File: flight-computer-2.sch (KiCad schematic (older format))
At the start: 80 parts

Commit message: Connecting interrupt pins
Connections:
- wire segments 211 -> 214
- no-connect marks 32 -> 29
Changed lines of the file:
@@
 Sheet 1 1
 Title "VTOL EDF Flight Computer"
-Date "2020-07-23"
+Date "2020-07-24"
 Rev "v2"
 Comp ""
@@
 NoConn ~ 9400 1750
 NoConn ~ 9400 1850
-NoConn ~ 7800 2650
-NoConn ~ 7800 2550
 NoConn ~ 9400 2250
 NoConn ~ 9400 2150
@@
 Wire Wire Line
 	4050 1900 4200 1900
-NoConn ~ 7800 2950
 Text Label 9550 2350 2    50   ~ 0
 IO10
@@
 Connection ~ 2600 5550
 Connection ~ 2600 5850
+Text Label 7500 2950 0    50   ~ 0
+IMU_INT
+Wire Wire Line
+	7500 2950 7800 2950
+Text Label 7450 2650 0    50   ~ 0
+ALT_INT_1
+Text Label 7450 2550 0    50   ~ 0
+ALT_INT_2
+Wire Wire Line
+	7450 2550 7800 2550
+Wire Wire Line
+	7450 2650 7800 2650
 $EndSCHEMATC

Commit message: Assigning footprints
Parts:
- D1, D3: renamed from D?; footprint (none) -> flight-computer-2:D_PowerDI-5
- D4, D5, D6: renamed from D?; footprint (none) -> flight-computer-2:D_SOD-523
- D9: renamed from D?; footprint (none) -> flight-computer-2:LED_Cree-PLCC4_2x2mm_CW
- E1: renamed from E?; footprint (none) -> flight-computer-2:ANT_PRO-OB-440
- J1: renamed from J?; footprint (none) -> flight-computer-2:GCT_USB4105-GF-A
- J2, J3, J4, J5, J6: renamed from J?; footprint (none) -> flight-computer-2:PinHeader_1x03_P2.54mm_Vertical
- J7, J8: renamed from J?; footprint (none) -> flight-computer-2:PinHeader_1x07_P2.54mm_Vertical
- SW1, SW2: renamed from SW?; footprint (none) -> flight-computer-2:SW_PTS810_SJM_250_SMTR_LFS
- U1: renamed from U?; footprint (none) -> flight-computer-2:SOT-223
- U2: renamed from U?; footprint (none) -> flight-computer-2:SOT-363_SC-70-6
- U3: renamed from U?; footprint (none) -> flight-computer-2:LGA-28_5.2x3.8mm_P0.5mm
- U4: renamed from U?; footprint (none) -> flight-computer-2:QFN-28-1EP_5x5mm_P0.5mm_EP3.35x3.35mm
- U5: renamed from U?; footprint (none) -> flight-computer-2:LGA-8_3x5mm_P1.25mm
- U6: renamed from U?; footprint (none) -> flight-computer-2:PQFN50P700X700X104-49N
- Y1: renamed from Y?; footprint (none) -> flight-computer-2:ABS07
- gave numbers to parts that had none: 56

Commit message: New USB ESD protection IC
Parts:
- removed D4, D5, D6: ESD5Z5.0T1G, flight-computer-2:D_SOD-523, symbol Device:D_TVS_ALT
- added D?: USBLC6-2SC6, Package_TO_SOT_SMD:SOT-23-6, symbol flight-computer-2:USBLC6-2SC6
- added R?: 1M, symbol Device:R_Small
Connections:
- wire segments 214 -> 219
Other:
- moved on the sheet: D3
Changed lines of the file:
@@
 $EndComp
 Wire Wire Line
-	1600 5750 1500 5750
-Wire Wire Line
-	1600 5950 1500 5950
-Connection ~ 1500 5950
+	1400 5950 1300 5950
+Connection ~ 1300 5950
 NoConn ~ 1600 5150
 NoConn ~ 1600 5250
@@
 	0    -1   -1   0
 $EndComp
-Wire Wire Line
-	2500 5450 2600 5450
-Wire Wire Line
-	2600 5450 2600 5550
-Wire Wire Line
-	2600 5550 2500 5550
-Wire Wire Line
-	2500 5750 2600 5750
-Wire Wire Line
-	2600 5750 2600 5850
-Wire Wire Line
-	2600 5850 2500 5850
-Text Label 3300 5150 2    50   ~ 0
+Text Label 3300 5050 2    50   ~ 0
 VIN
 Wire Wire Line
-	3300 5150 3150 5150
-$Comp
-L Device:D_TVS_ALT D6
-U 1 1 5F108BF7
-P 3000 5850
-F 0 "D6" H 3000 6000 50  0000 C CNN
-F 1 "ESD5Z5.0T1G" H 3000 6100 50  0000 C CNN
-F 2 "flight-computer-2:D_SOD-523" H 3000 5850 50  0001 C CNN
-F 3 "~" H 3000 5850 50  0001 C CNN
-F 4 "ESD5Z5.0T1G" H 3000 5850 50  0001 C CNN "MPN"
-	1    3000 5850
-	-1   0    0    1
-$EndComp
+	3300 5050 3150 5050
 $Comp
 L Device:D_Schottky_ALT D3
 U 1 1 5F10A2FB
-P 3000 5150
-F 0 "D3" H 3000 4934 50  0000 C CNN
-F 1 "PDS4150-13" H 3000 5025 50  0000 C CNN
-F 2 "flight-computer-2:D_PowerDI-5" H 3000 5150 50  0001 C CNN
-F 3 "~" H 3000 5150 50  0001 C CNN
-F 4 "PDS4150-13" H 3000 5150 50  0001 C CNN "MPN"
-	1    3000 5150
+P 3000 5050
+F 0 "D3" H 3000 4834 50  0000 C CNN
+F 1 "PDS4150-13" H 3000 4925 50  0000 C CNN
+F 2 "flight-computer-2:D_PowerDI-5" H 3000 5050 50  0001 C CNN
+F 3 "~" H 3000 5050 50  0001 C CNN
+F 4 "PDS4150-13" H 3000 5050 50  0001 C CNN "MPN"
+	1    3000 5050
 	-1   0    0    1
 $EndComp
-Wire Wire Line
-	2600 5550 2850 5550
-Wire Wire Line
-	2600 5850 2850 5850
-$Comp
-L Device:D_TVS_ALT D5
-U 1 1 5F11064B
-P 3000 5550
-F 0 "D5" H 3000 5650 50  0000 C CNN
-F 1 "ESD5Z5.0T1G" H 3000 5750 50  0000 C CNN
-F 2 "flight-computer-2:D_SOD-523" H 3000 5550 50  0001 C CNN
-F 3 "~" H 3000 5550 50  0001 C CNN
-F 4 "ESD5Z5.0T1G" H 3000 5550 50  0001 C CNN "MPN"
-	1    3000 5550
-	-1   0    0    1
-$EndComp
-Text Label 2700 5850 0    50   ~ 0
+Text Label 3400 5750 2    50   ~ 0
 D-
-Text Label 2700 5550 0    50   ~ 0
+Text Label 3400 5550 2    50   ~ 0
 D+
 $Comp
@@
 $EndComp
 Wire Wire Line
-	1500 5750 1500 5850
-Wire Wire Line
-	1600 5850 1500 5850
-Connection ~ 1500 5850
-Wire Wire Line
-	1500 5850 1500 5950
+	1300 5750 1300 5850
+Connection ~ 1300 5850
+Wire Wire Line
+	1300 5850 1300 5950
 $Comp
 L power:GND #PWR0118
 U 1 1 5F2FC5FB
-P 1500 6050
-F 0 "#PWR0118" H 1500 5800 50  0001 C CNN
-F 1 "GND" H 1505 5877 50  0000 C CNN
-F 2 "" H 1500 6050 50  0001 C CNN
-F 3 "" H 1500 6050 50  0001 C CNN
-	1    1500 6050
+P 1300 6050
+F 0 "#PWR0118" H 1300 5800 50  0001 C CNN
+F 1 "GND" H 1305 5877 50  0000 C CNN
+F 2 "" H 1300 6050 50  0001 C CNN
+F 3 "" H 1300 6050 50  0001 C CNN
+	1    1300 6050
 	1    0    0    -1
 $EndComp
@@
 $EndComp
 $Comp
-L Device:D_TVS_ALT D4
-U 1 1 5F10B283
-P 3000 5250
-F 0 "D4" H 2950 5350 50  0000 L CNN
-F 1 "ESD5Z5.0T1G" H 2750 5450 50  0000 L CNN
-F 2 "flight-computer-2:D_SOD-523" H 3000 5250 50  0001 C CNN
-F 3 "~" H 3000 5250 50  0001 C CNN
-F 4 "ESD5Z5.0T1G" H 3000 5250 50  0001 C CNN "MPN"
-	1    3000 5250
-	-1   0    0    1
-$EndComp
-$Comp
 L power:GND #PWR0119
 U 1 1 5F384159
@@
 $EndComp
 Connection ~ 8050 6050
-$Comp
-L power:GND #PWR0120
-U 1 1 5F3CFF34
-P 3150 5250
-F 0 "#PWR0120" H 3150 5000 50  0001 C CNN
-F 1 "GND" V 3155 5122 50  0000 R CNN
-F 2 "" H 3150 5250 50  0001 C CNN
-F 3 "" H 3150 5250 50  0001 C CNN
-	1    3150 5250
-	0    -1   -1   0
-$EndComp
-$Comp
-L power:GND #PWR0121
-U 1 1 5F3D04B5
-P 3150 5550
-F 0 "#PWR0121" H 3150 5300 50  0001 C CNN
-F 1 "GND" V 3155 5422 50  0000 R CNN
-F 2 "" H 3150 5550 50  0001 C CNN
-F 3 "" H 3150 5550 50  0001 C CNN
-	1    3150 5550
-	0    -1   -1   0
-$EndComp
-$Comp
-L power:GND #PWR0122
-U 1 1 5F3D0830
-P 3150 5850
-F 0 "#PWR0122" H 3150 5600 50  0001 C CNN
-F 1 "GND" V 3155 5722 50  0000 R CNN
-F 2 "" H 3150 5850 50  0001 C CNN
-F 3 "" H 3150 5850 50  0001 C CNN
-	1    3150 5850
-	0    -1   -1   0
-$EndComp
 $Comp
 L flight-computer-2:ESP32-PICO-D4 U6
@@
 Connection ~ 2700 1400
 Wire Wire Line
-	1500 5950 1500 6050
-Wire Wire Line
-	2850 5150 2850 5250
+	1300 5950 1300 6050
+Wire Wire Line
+	2850 5050 2850 5150
 Wire Wire Line
 	2500 5150 2600 5150
@@
 	2600 5250 2500 5250
 Wire Wire Line
-	2600 5250 2850 5250
-Connection ~ 2850 5250
+	2600 5150 2850 5150
 $Comp
 L power:PWR_FLAG #FLG0101
@@
 Wire Wire Line
 	9900 1450 10250 1450
-Connection ~ 2600 5250
-Connection ~ 2600 5550
-Connection ~ 2600 5850
 Text Label 7500 2950 0    50   ~ 0
 IMU_INT
@@
 Wire Wire Line
 	7450 2650 7800 2650
+$Comp
+L Device:R_Small R?
+U 1 1 5F20CB9C
+P 1500 5950
+F 0 "R?" V 1400 5950 50  0000 C CNN
+F 1 "1M" V 1300 5950 50  0000 C CNN
+F 2 "" H 1500 5950 50  0001 C CNN
+F 3 "~" H 1500 5950 50  0001 C CNN
+	1    1500 5950
+	0    -1   -1   0
+$EndComp
+Wire Wire Line
+	1300 5750 1600 5750
+Wire Wire Line
+	1300 5850 1600 5850
+Wire Wire Line
+	2500 5450 2600 5450
+Wire Wire Line
+	2600 5450 2600 5550
+Wire Wire Line
+	2600 5550 2500 5550
+Wire Wire Line
+	2500 5750 2600 5750
+Wire Wire Line
+	2600 5750 2600 5850
+Wire Wire Line
+	2600 5850 2500 5850
+Connection ~ 2600 5550
+$Comp
+L flight-computer-2:USBLC6-2SC6 D?
+U 1 1 5F45F25E
+P 3000 5850
+F 0 "D?" H 3000 5750 50  0000 C CNN
+F 1 "USBLC6-2SC6" H 3000 5650 50  0000 C CNN
+F 2 "Package_TO_SOT_SMD:SOT-23-6" H 3200 5850 50  0001 L BNN
+F 3 "~" H 3200 5850 50  0001 L BNN
+	1    3000 5850
+	1    0    0    -1
+$EndComp
+Wire Wire Line
+	2600 5550 2700 5550
+Connection ~ 2600 5150
+$Comp
+L power:GND #PWR?
+U 1 1 5F510CC3
+P 2700 5350
+F 0 "#PWR?" H 2700 5100 50  0001 C CNN
+F 1 "GND" V 2705 5222 50  0000 R CNN
+F 2 "" H 2700 5350 50  0001 C CNN
+F 3 "" H 2700 5350 50  0001 C CNN
+	1    2700 5350
+	0    1    1    0
+$EndComp
+Wire Wire Line
+	2600 5750 2700 5750
+Connection ~ 2600 5750
+Wire Wire Line
+	2850 5150 3400 5150
+Connection ~ 2850 5150
+Wire Wire Line
+	3300 5350 3400 5350
+Wire Wire Line
+	3400 5350 3400 5150
+Wire Wire Line
+	3300 5550 3400 5550
+Wire Wire Line
+	3300 5750 3400 5750
 $EndSCHEMATC

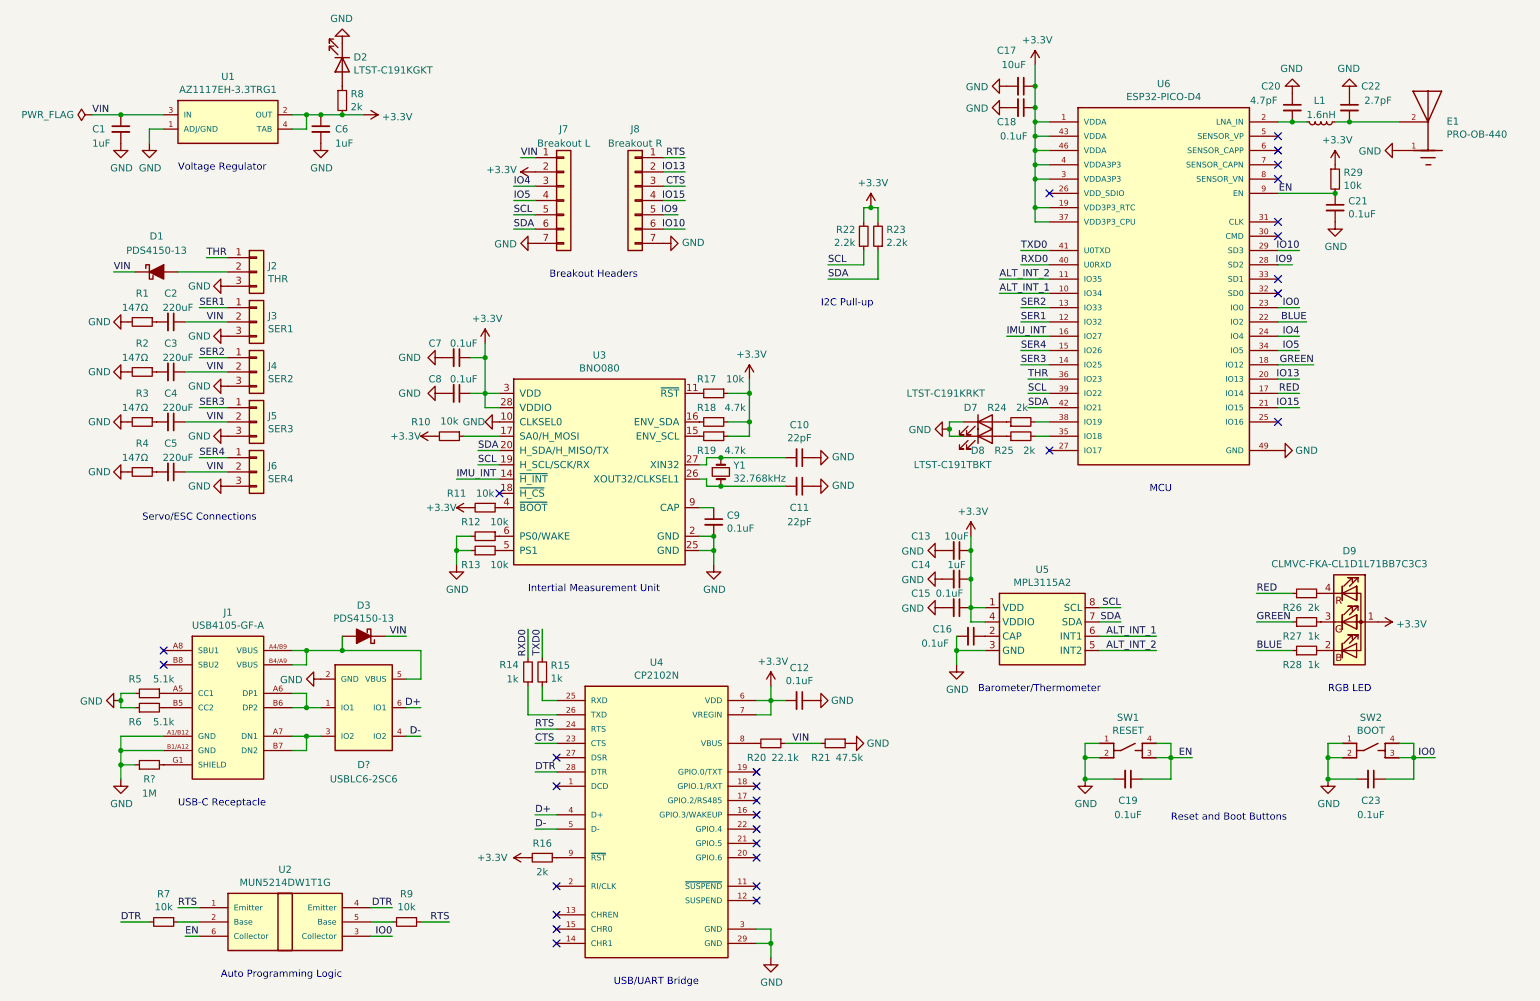
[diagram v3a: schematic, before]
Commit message: New antenna
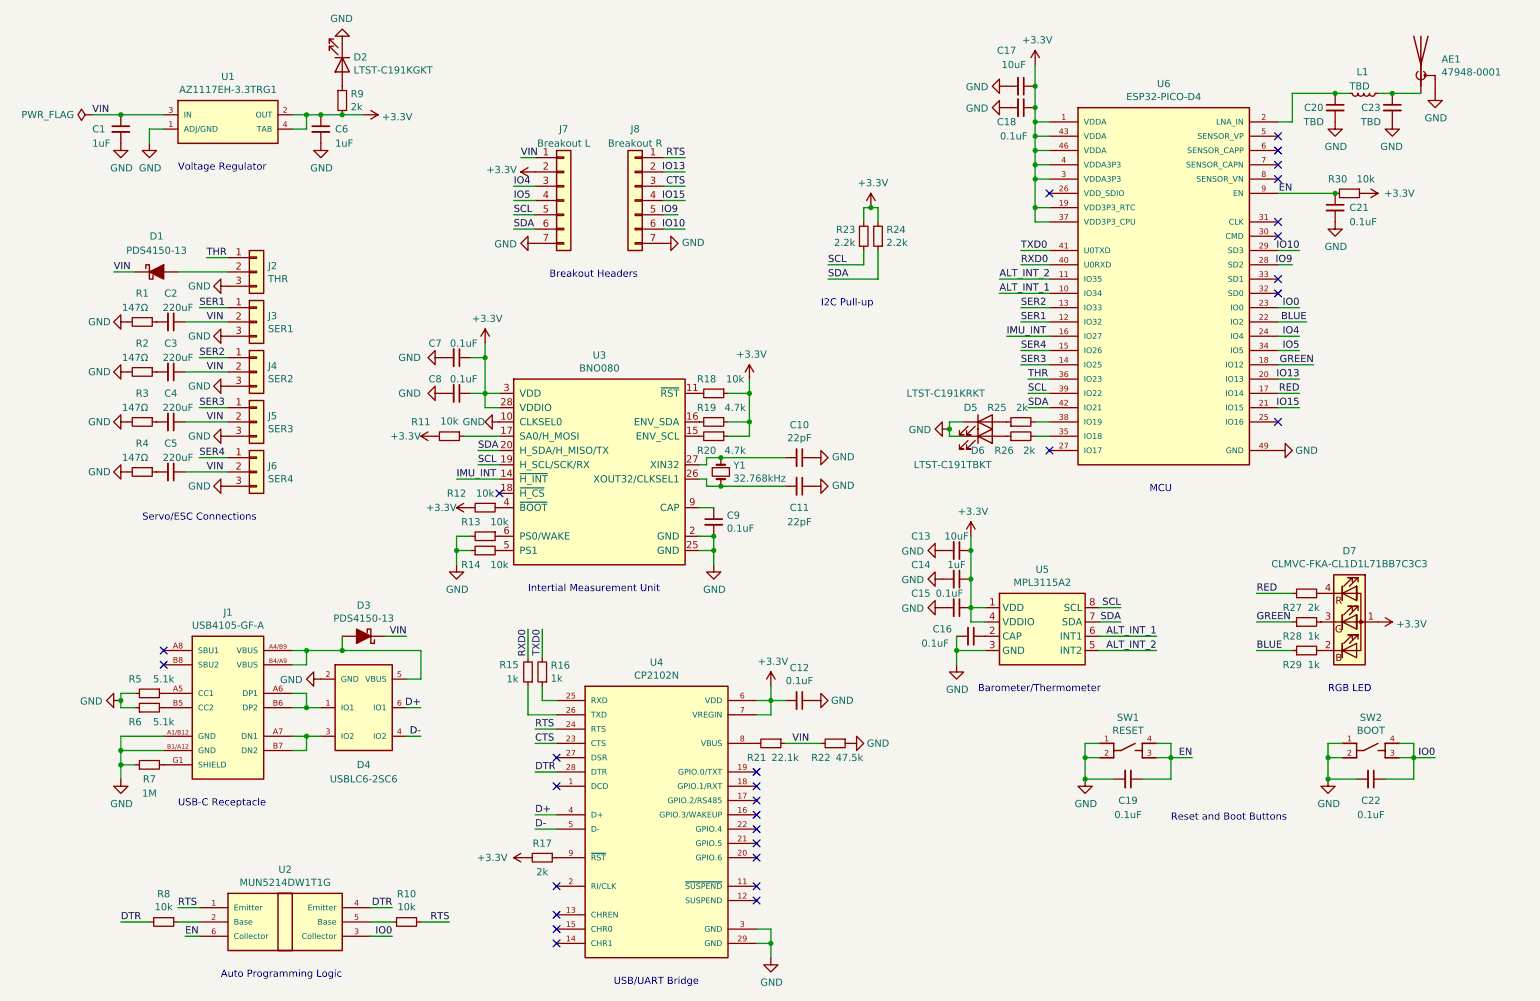
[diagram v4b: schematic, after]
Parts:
- removed E1: PRO-OB-440, flight-computer-2:ANT_PRO-OB-440, symbol flight-computer-2:PRO-OB-440
- added AE1: 47948-0001, symbol flight-computer-2:47948-0001
- C20: value 4.7pF -> TBD
- C23: renamed from C22; value 2.7pF -> TBD
- D4: renamed from D?; MPN (none) -> USBLC6-2SC6
- L1: value 1.6nH -> TBD
- gave numbers to parts that had none: 1
- renumbered C23 to C22, D7 to D5, D8 to D6, D9 to D7, R9 to R10, R10 to R11, R11 to R12, R12 to R13, R13 to R14, R14 to R15, R15 to R16, R16 to R17, R17 to R18, R18 to R19, R19 to R20, R20 to R21, R21 to R22, R22 to R23, R23 to R24, R24 to R25, R25 to R26, R26 to R27, R27 to R28, R28 to R29, R29 to R30, R7 to R8, R8 to R9
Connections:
- net GND: now also C20.2, C23.2, AE1.2 (PAD1), AE1.3 (PAD2), AE1.4 (PAD3); no longer C20.1, C23.1
- net at L1.2, U6.2 (LNA_IN): now also C20.1; no longer C20.2
- net at L1.1: now also C23.1, AE1.1 (FEED); no longer C23.2
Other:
- moved on the sheet: C20, C23, L1, R30

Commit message: Assigning footprints
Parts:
- AE1: footprint (none) -> flight-computer-2:47948-0001
- C1, C10, C11, C12, C13, C14, C15, C16, C17, C18, C19, C2, C21, C22, C3, C4, C5, C6, C7, C8, C9: footprint (none) -> flight-computer-2:C_0603_1608Metric
- C20, C23: value TBD -> DNP; footprint (none) -> flight-computer-2:C_0402_1005Metric
- D2, D5, D6: footprint (none) -> flight-computer-2:LED_0603_1608Metric
- L1: value TBD -> 0K; footprint (none) -> flight-computer-2:L_0402_1005Metric
- R1, R10, R11, R12, R13, R14, R15, R16, R17, R18, R19, R2, R20, R21, R22, R23, R24, R25, R26, R27, R28, R29, R3, R30, R4, R5, R6, R7, R8, R9: footprint (none) -> flight-computer-2:R_0603_1608Metric

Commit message: New voltage regulator and diode
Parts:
- C1, C6: value 1uF -> 4.7uF
- D1, D3: value PDS4150-13 -> SM5817PL-TP
- U1: value AZ1117EH-3.3TRG1 -> AP2114H-3.3TRG1; symbol flight-computer-2:AZ1117EH-3.3TRG1 -> flight-computer-2:AP2114H-3.3TRG1; MPN AZ1117EH-3.3TRG1 -> AP2114H-3.3TRG1
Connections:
- net IO5: no longer J7.4 (Pin_4), U6.34 (IO5)
- net VIN: no longer C2.1, C3.1, C4.1, C5.1, J3.2 (Pin_2), J4.2 (Pin_2), J5.2 (Pin_2), J6.2 (Pin_2)
- net VBEC: now reaches D1.2 (A), J2.2 (Pin_2)
- net VBEC: now also C2.1, C3.1, C4.1, C5.1, J3.2 (Pin_2), J4.2 (Pin_2), J5.2 (Pin_2), J6.2 (Pin_2)
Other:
- moved on the sheet: D1
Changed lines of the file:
@@
 P 3000 5050
 F 0 "D3" H 3000 4834 50  0000 C CNN
-F 1 "PDS4150-13" H 3000 4925 50  0000 C CNN
+F 1 "SM5817PL-TP" H 3000 4925 50  0000 C CNN
 F 2 "flight-computer-2:D_PowerDI-5" H 3000 5050 50  0001 C CNN
 F 3 "~" H 3000 5050 50  0001 C CNN
@@
 P 2700 1500
 F 0 "C6" H 2800 1500 50  0000 L CNN
-F 1 "1uF" H 2800 1400 50  0000 L CNN
+F 1 "4.7uF" H 2800 1400 50  0000 L CNN
 F 2 "flight-computer-2:C_0603_1608Metric" H 2700 1500 50  0001 C CNN
 F 3 "~" H 2700 1500 50  0001 C CNN
@@
 P 1300 1500
 F 0 "C1" H 1100 1500 50  0000 L CNN
-F 1 "1uF" H 1100 1400 50  0000 L CNN
+F 1 "4.7uF" H 1050 1400 50  0000 L CNN
 F 2 "flight-computer-2:C_0603_1608Metric" H 1300 1500 50  0001 C CNN
 F 3 "~" H 1300 1500 50  0001 C CNN
@@
 $EndComp
 $Comp
-L flight-computer-2:AZ1117EH-3.3TRG1 U1
+L flight-computer-2:AP2114H-3.3TRG1 U1
 U 1 1 5F13844B
 P 2050 1500
 F 0 "U1" H 2050 1867 50  0000 C CNN
-F 1 "AZ1117EH-3.3TRG1" H 2050 1776 50  0000 C CNN
+F 1 "AP2114H-3.3TRG1" H 2050 1776 50  0000 C CNN
 F 2 "flight-computer-2:SOT-223" H 1650 1300 50  0001 L BNN
 F 3 "~" H 2000 1200 50  0001 L BNN
-F 4 "AZ1117EH-3.3TRG1" H 2050 1500 50  0001 C CNN "MPN"
+F 4 "AP2114H-3.3TRG1" H 2050 1500 50  0001 C CNN "MPN"
 	1    2050 1500
 	1    0    0    -1
@@
 L Device:D_Schottky_ALT D1
 U 1 1 5F77575B
-P 1550 2500
-F 0 "D1" H 1550 2750 50  0000 C CNN
-F 1 "PDS4150-13" H 1550 2650 50  0000 C CNN
-F 2 "flight-computer-2:D_PowerDI-5" H 1550 2500 50  0001 C CNN
-F 3 "~" H 1550 2500 50  0001 C CNN
-F 4 "PDS4150-13" H 1550 2500 50  0001 C CNN "MPN"
-	1    1550 2500
-	1    0    0    -1
-$EndComp
-Text Label 1250 2500 0    50   ~ 0
-VIN
-Wire Wire Line
-	1250 2500 1400 2500
-Wire Wire Line
-	1700 2500 2050 2500
+P 1600 2500
+F 0 "D1" H 1600 2750 50  0000 C CNN
+F 1 "SM5817PL-TP" H 1600 2650 50  0000 C CNN
+F 2 "flight-computer-2:D_PowerDI-5" H 1600 2500 50  0001 C CNN
+F 3 "~" H 1600 2500 50  0001 C CNN
+F 4 "PDS4150-13" H 1600 2500 50  0001 C CNN "MPN"
+	1    1600 2500
+	1    0    0    -1
+$EndComp
+Wire Wire Line
+	1750 2500 2050 2500
 $Comp
 L power:GND #PWR09
@@
 $EndComp
 Text Label 1900 2850 0    50   ~ 0
-VIN
+VBEC
 Text Label 1900 3200 0    50   ~ 0
-VIN
+VBEC
 Text Label 1900 3550 0    50   ~ 0
-VIN
+VBEC
 Text Label 1900 3900 0    50   ~ 0
-VIN
+VBEC
 Wire Wire Line
 	1750 2850 2050 2850
@@
 Text Label 9550 2950 2    50   ~ 0
 IO4
-Text Label 9550 3050 2    50   ~ 0
+Text Label 9950 3050 2    50   ~ 0
 IO5
 Wire Wire Line
 	9400 2950 9550 2950
 Wire Wire Line
-	9400 3050 9550 3050
+	9800 3050 9950 3050
 Text Label 4050 1900 0    50   ~ 0
 IO4
-Text Label 4050 2000 0    50   ~ 0
+Text Label 3650 2000 0    50   ~ 0
 IO5
 Wire Wire Line
-	4050 2000 4200 2000
+	3650 2000 3800 2000
 Wire Wire Line
 	4050 1900 4200 1900
@@
 $EndComp
 Connection ~ 9800 1950
+Text Label 1900 2500 0    50   ~ 0
+VBEC
+Wire Wire Line
+	1300 2500 1450 2500
+Text Label 1300 2500 0    50   ~ 0
+VIN
 $EndSCHEMATC
